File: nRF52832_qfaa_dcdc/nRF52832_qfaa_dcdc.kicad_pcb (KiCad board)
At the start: 2 copper layers, 20 x 14 mm, 20 parts, among them U1 NRF52832, X1 32MHz, X2 32.768kHz

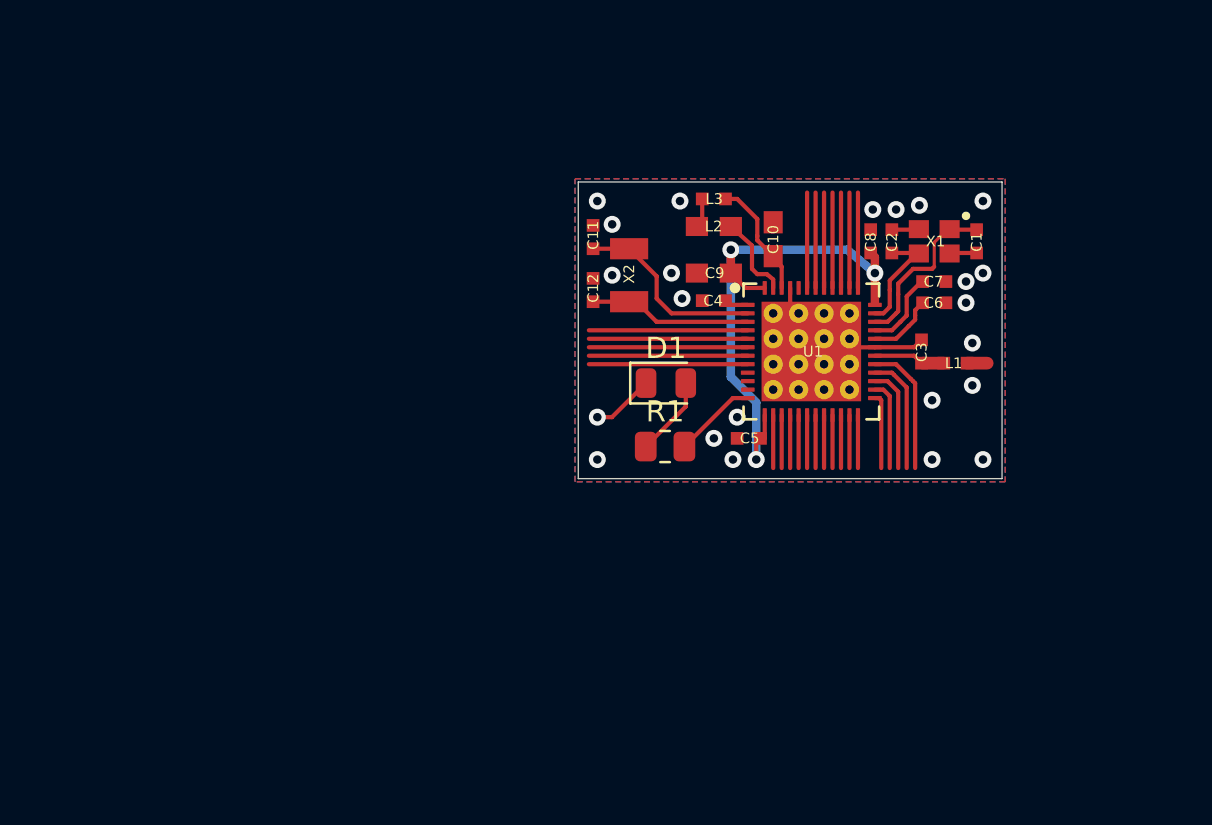
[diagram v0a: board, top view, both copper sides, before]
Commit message: Mapping pour bouton et buzzer
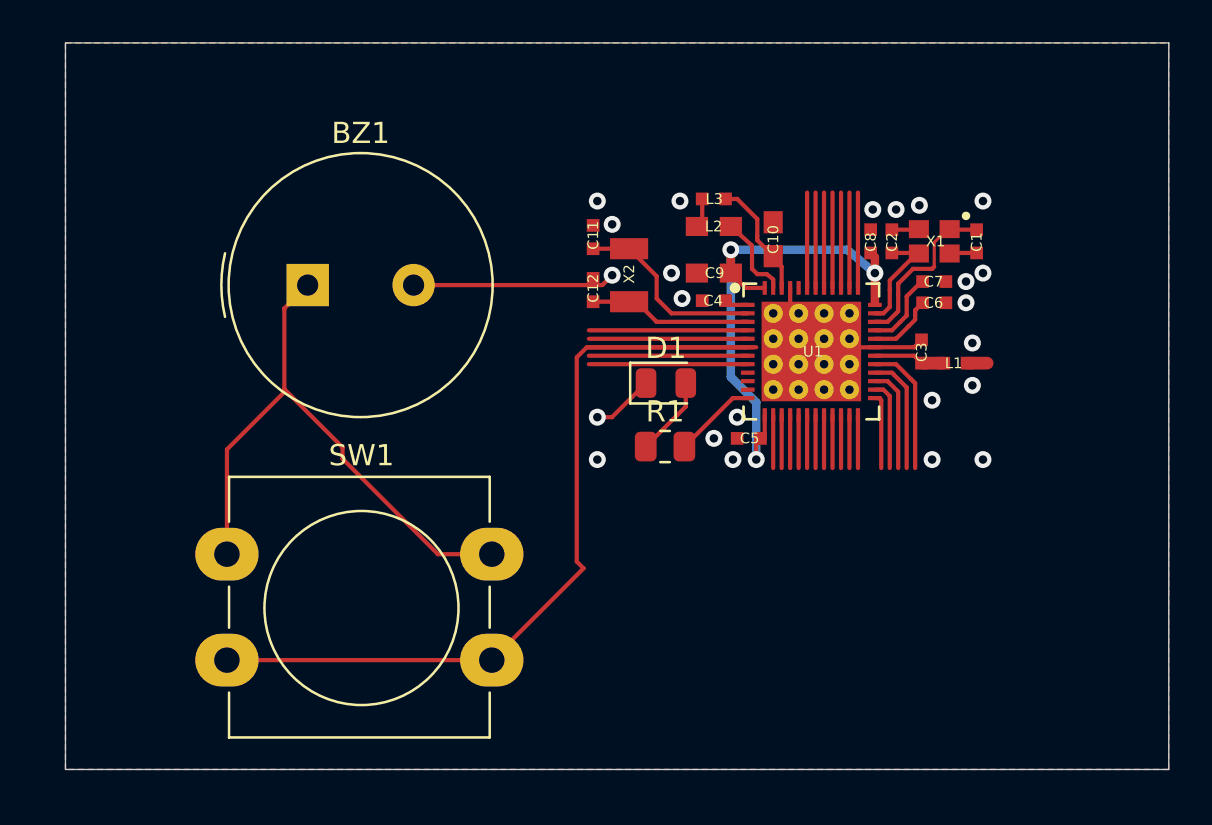
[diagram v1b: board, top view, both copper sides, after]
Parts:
- added BZ1: Buzzer, Buzzer_Beeper:Buzzer_TDK_PS1240P02BT_D12.2mm_H6.5mm, F.Cu at (125.7, 102.9)
- added SW1: SW_Push, Button_Switch_THT:SW_PUSH-12mm_Wuerth-430476085716, F.Cu at (121.9, 115.6)
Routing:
- net /P0.04: track 7.50 -> 44.9 mm
- net Net-(BZ1--): track 0.00 -> 27.6 mm
- net GND: track 30.0 -> 39.6 mm
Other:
- board size 20 x 14 mm -> 52.1 x 34.3 mm

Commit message: commit changement elec
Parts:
- added BT1: Battery_Cell, Buzzer_Beeper:Buzzer_Mallory_AST1240MLQ, B.Cu at (139.1, 109.9)
- added J1: Conn_ARM_SWD_TagConnect_TC2030-NL, Connector:Tag-Connect_TC2030-IDC-NL_2x03_P1.27mm_Vertical, F.Cu at (161.0, 111.1)
- BZ1: footprint Buzzer_Beeper:Buzzer_TDK_PS1240P02BT_D12.2mm_H6.5mm -> Buzzer_Beeper:Buzzer_Mallory_AST1240MLQ
- SW1: footprint Button_Switch_THT:SW_PUSH-12mm_Wuerth-430476085716 -> Button_Switch_THT:SW_CW_GPTS203211B
- moved C12 25.1 mm to (114.1, 103.5), turned to 0 degrees
- moved SW1 20.3 mm to (142.2, 115.5)
- moved BZ1 16.4 mm to (136.2, 115.5)
- moved D1 13.9 mm to (129.2, 111.1), turned to -90 degrees
- moved R1 1.91 mm to (142.6, 108.6)
- moved C5 0.50 mm to (146.1, 110.1)
- moved C4 0.24 mm to (144.7, 103.6)
- moved C9 0.24 mm to (144.7, 102.3)
- moved L2 0.24 mm to (144.7, 100.1)
- moved L3 0.24 mm to (144.7, 98.8)
- moved U1 0.24 mm to (149.3, 106.0)
- moved X2 0.24 mm to (140.7, 102.4)
- moved C1 0.24 mm to (157.1, 100.8)
- moved C10 0.24 mm to (147.5, 100.7)
- moved C11 0.24 mm to (139.0, 100.6)
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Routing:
- net VCC: track 25.6 -> 68.9 mm, vias 3 -> 4
- net /SWDCLK: track 3.54 -> 20.8 mm
- net /SWDIO: track 4.22 -> 18.0 mm
- net /P0.21/RESET: track 2.50 -> 16.2 mm, vias 0 -> 2
- net Net-(BZ1--): track 27.6 -> 14.1 mm
- net /P0.22: track 4.91 -> 16.3 mm, vias 0 -> 2
- net Net-(D1-A): track 3.78 -> 13.9 mm
- net /P0.04: track 44.9 -> 37.3 mm
- net /P0.06: track 7.50 -> 0.00 mm
- net /P0.03: track 7.50 -> 0.00 mm
- net /P0.02: track 7.50 -> 0.00 mm
- net /P0.05: track 7.50 -> 0.66 mm
- net /P0.31: track 4.50 -> 0.00 mm
- net /P0.25: track 4.50 -> 9.00 mm
- net Net-(U1-DCC@47): track 4.04 -> 0.00 mm
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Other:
- board size 52.1 x 34.3 mm -> 37.8 x 30 mm
